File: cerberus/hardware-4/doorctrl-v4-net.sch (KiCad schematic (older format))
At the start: 40 parts, among them CON6 RJHSE-5085, U4 ENC28J60, U5 MC34063, U9 BCR08PN, X2 25MHz

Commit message: Various cleanups
git-svn-id: file:///home/ff/projects/osaa/svn@255 a092026d-3e22-4cff-94a7-eaa6fdd35d37
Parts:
- C37: value 100uF -> 220uF
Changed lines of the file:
@@
-EESchema Schematic File Version 2  date 2011-01-03T16:40:54 CET
+EESchema Schematic File Version 2  date 2011-01-17T19:42:11 CET
 LIBS:enc28j60
 LIBS:power
@@
 Sheet 2 6
 Title ""
-Date "3 jan 2011"
+Date "17 jan 2011"
 Rev ""
 Comp ""
@@
 P 6550 6450
 F 0 "C37" H 6600 6550 50  0000 L CNN
-F 1 "100uF" H 6600 6350 50  0000 L CNN
+F 1 "220uF" H 6600 6350 50  0000 L CNN
 	1    6550 6450
 	1    0    0    -1

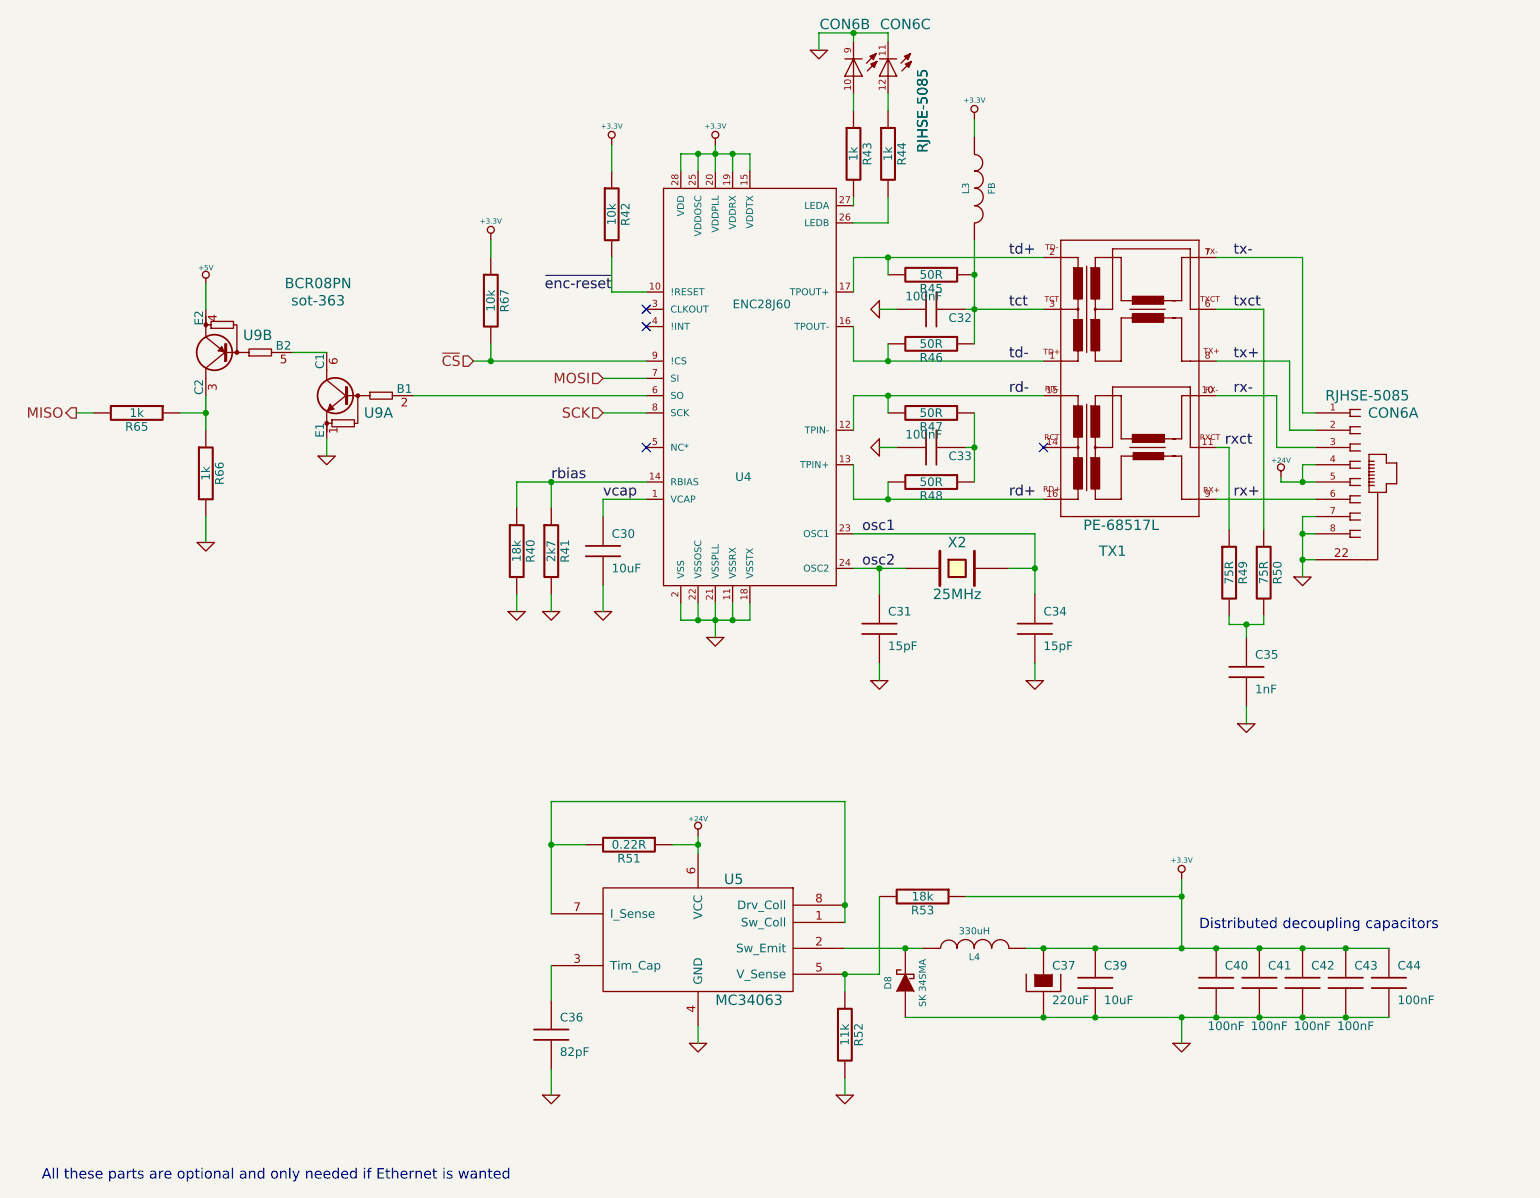
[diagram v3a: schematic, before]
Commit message: Fixed a couple of bugs: No more level shifter and rfid carrier wave output is connected correctly
git-svn-id: file:///home/ff/projects/osaa/svn@258 a092026d-3e22-4cff-94a7-eaa6fdd35d37
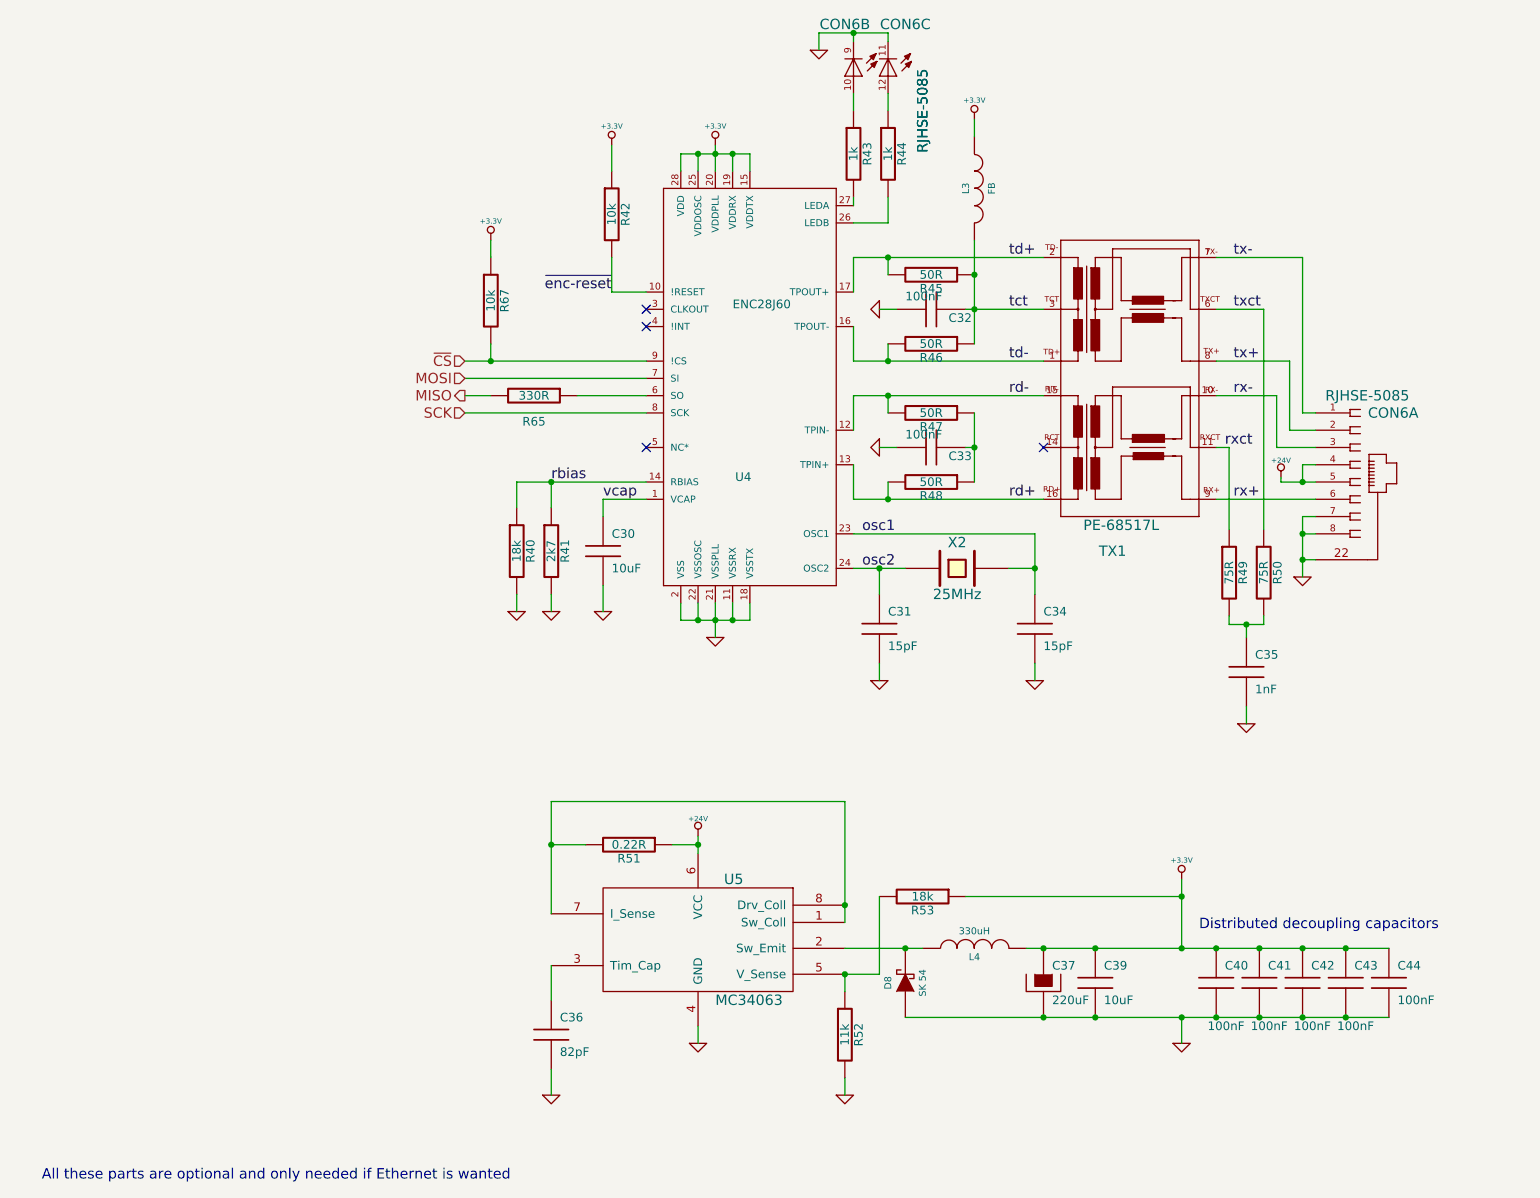
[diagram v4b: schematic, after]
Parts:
- removed R66: 1k, symbol R
- removed U9: BCR08PN, sot-363, symbol NPN/PNP
- D8: value SK 34SMA -> SK 54
- R65: value 1k -> 330R
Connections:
- net at U4.6 (SO): now also R65.1
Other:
- moved on the sheet: R65
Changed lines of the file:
@@
-EESchema Schematic File Version 2  date 2011-01-17T20:19:18 CET
+EESchema Schematic File Version 2  date 2011-01-23T22:09:23 CET
 LIBS:enc28j60
 LIBS:power
@@
 Sheet 2 6
 Title ""
-Date "17 jan 2011"
+Date "23 jan 2011"
 Rev ""
 Comp ""
@@
 $EndDescr
 Wire Wire Line
-	950  3150 1050 3150
-Wire Wire Line
-	1700 3250 1700 3050
-Wire Wire Line
-	1700 2400 1700 2550
-Wire Wire Line
-	2400 3400 2400 3300
+	3200 3050 3350 3050
 Wire Wire Line
 	3350 2150 3350 2250
 Wire Wire Line
-	3250 2850 4250 2850
-Wire Wire Line
-	6550 2550 6100 2550
-Wire Wire Line
-	6550 3050 5450 3050
+	3200 2850 3350 2850
+Wire Wire Line
+	3350 2850 4250 2850
+Wire Wire Line
+	6550 2550 6150 2550
+Wire Wire Line
+	6150 2550 6100 2550
+Wire Wire Line
+	6550 3050 5650 3050
+Wire Wire Line
+	5650 3050 5450 3050
 Connection ~ 8050 4000
 Wire Wire Line
 	8050 4000 8125 4000
 Wire Wire Line
-	8550 6250 6450 6250
-Wire Wire Line
-	7350 6250 7350 5850
+	8550 6250 8300 6250
+Wire Wire Line
+	8300 6250 8050 6250
+Wire Wire Line
+	8050 6250 7800 6250
+Wire Wire Line
+	7800 6250 7550 6250
+Wire Wire Line
+	7550 6250 7350 6250
+Wire Wire Line
+	7350 6250 6850 6250
+Wire Wire Line
+	6850 6250 6550 6250
+Wire Wire Line
+	6550 6250 6450 6250
+Wire Wire Line
+	7350 6250 7350 5950
+Wire Wire Line
+	7350 5950 7350 5850
 Connection ~ 7350 6650
 Wire Wire Line
@@
 Connection ~ 5750 6250
 Wire Wire Line
-	5850 6250 5400 6250
+	5850 6250 5750 6250
+Wire Wire Line
+	5750 6250 5400 6250
 Connection ~ 5400 6400
 Wire Wire Line
@@
 Connection ~ 5400 6000
 Wire Wire Line
-	5400 6100 5400 5400
-Wire Wire Line
-	4550 5600 4550 5700
-Wire Wire Line
-	3700 6050 3700 5400
+	5400 6100 5400 6000
+Wire Wire Line
+	5400 6000 5400 5400
+Wire Wire Line
+	4550 5600 4550 5650
+Wire Wire Line
+	4550 5650 4550 5700
+Wire Wire Line
+	3700 6050 3700 5650
+Wire Wire Line
+	3700 5650 3700 5400
 Wire Wire Line
 	3700 5400 5400 5400
@@
 	7825 4325 7825 4375
 Wire Wire Line
-	7825 4375 7625 4375
+	7825 4375 7725 4375
+Wire Wire Line
+	7725 4375 7625 4375
 Wire Wire Line
 	7725 4950 7725 4850
@@
 	8125 3650 7550 3650
 Wire Wire Line
-	6150 3150 6150 3550
+	6150 3150 6150 3350
+Wire Wire Line
+	6150 3350 6150 3550
 Connection ~ 5650 3650
 Wire Wire Line
@@
 	5650 1000 5650 950
 Wire Wire Line
-	5650 950  5250 950
+	5650 950  5450 950
+Wire Wire Line
+	5450 950  5250 950
 Wire Wire Line
 	5250 950  5250 1050
@@
 	6500 4600 6500 4700
 Wire Wire Line
-	5750 4050 5450 4050
-Wire Wire Line
-	6500 4200 6500 3850
+	5750 4050 5600 4050
+Wire Wire Line
+	5600 4050 5450 4050
+Wire Wire Line
+	6500 4200 6500 4050
+Wire Wire Line
+	6500 4050 6500 3850
 Wire Wire Line
 	6500 3850 5450 3850
@@
 	4000 3650 4000 3750
 Wire Wire Line
-	4250 3550 3500 3550
+	4250 3550 3700 3550
+Wire Wire Line
+	3700 3550 3500 3550
 Wire Wire Line
 	3500 3550 3500 3700
@@
 	4750 1750 4750 1650
 Wire Wire Line
-	4650 1600 4650 1750
+	4650 1600 4650 1650
+Wire Wire Line
+	4650 1650 4650 1750
 Wire Wire Line
 	4450 1750 4450 1650
 Connection ~ 4750 4350
 Wire Wire Line
-	4850 4350 4450 4350
+	4850 4350 4750 4350
+Wire Wire Line
+	4750 4350 4650 4350
+Wire Wire Line
+	4650 4350 4550 4350
+Wire Wire Line
+	4550 4350 4450 4350
 Wire Wire Line
 	4850 4350 4850 4250
 Connection ~ 4650 4350
 Wire Wire Line
-	4650 4250 4650 4450
+	4650 4250 4650 4350
+Wire Wire Line
+	4650 4350 4650 4450
 Wire Wire Line
 	4450 4350 4450 4250
@@
 	4850 1750 4850 1650
 Wire Wire Line
-	4850 1650 4450 1650
+	4850 1650 4750 1650
+Wire Wire Line
+	4750 1650 4650 1650
+Wire Wire Line
+	4650 1650 4550 1650
+Wire Wire Line
+	4550 1650 4450 1650
 Connection ~ 4650 1650
 Wire Wire Line
@@
 	5650 1300 5650 1400
 Wire Wire Line
-	6150 2150 6150 2750
+	6150 2150 6150 2350
+Wire Wire Line
+	6150 2350 6150 2550
+Wire Wire Line
+	6150 2550 6150 2750
 Connection ~ 6150 2350
 Wire Wire Line
@@
 	7925 3525 7925 3550
 Wire Wire Line
-	7925 3550 8125 3550
+	7925 3550 8050 3550
+Wire Wire Line
+	8050 3550 8125 3550
 Connection ~ 8050 3550
 Wire Wire Line
-	5750 6650 8550 6650
-Wire Wire Line
-	8050 3750 8050 4100
-Wire Wire Line
-	5450 3650 6550 3650
-Wire Wire Line
-	5450 2850 6550 2850
-Wire Wire Line
-	5450 2250 6550 2250
-Wire Wire Line
-	4250 3150 4000 3150
-Wire Wire Line
-	4250 2950 4000 2950
+	5750 6650 6550 6650
+Wire Wire Line
+	6550 6650 6850 6650
+Wire Wire Line
+	6850 6650 7350 6650
+Wire Wire Line
+	7350 6650 7550 6650
+Wire Wire Line
+	7550 6650 7800 6650
+Wire Wire Line
+	7800 6650 8050 6650
+Wire Wire Line
+	8050 6650 8300 6650
+Wire Wire Line
+	8300 6650 8550 6650
+Wire Wire Line
+	8050 3750 8050 3850
+Wire Wire Line
+	8050 3850 8050 4000
+Wire Wire Line
+	8050 4000 8050 4100
+Wire Wire Line
+	5450 3650 5650 3650
+Wire Wire Line
+	5650 3650 6550 3650
+Wire Wire Line
+	5450 2850 5650 2850
+Wire Wire Line
+	5650 2850 6550 2850
+Wire Wire Line
+	5450 2250 5650 2250
+Wire Wire Line
+	5650 2250 6550 2250
+Wire Wire Line
+	4250 3150 3200 3150
+Wire Wire Line
+	4250 2950 3200 2950
 Wire Wire Line
 	3350 2750 3350 2850
 Connection ~ 3350 2850
 Wire Wire Line
-	2900 3050 4250 3050
-Wire Wire Line
-	2400 2800 2200 2800
-Wire Wire Line
-	1700 3750 1700 3900
-Wire Wire Line
-	1550 3150 1700 3150
-Connection ~ 1700 3150
-$Comp
-L GND #PWR017
-U 1 1 4D21B7E7
-P 1700 3900
-F 0 "#PWR017" H 1700 3900 30  0001 C CNN
-F 1 "GND" H 1700 3830 30  0001 C CNN
-	1    1700 3900
-	1    0    0    -1
-$EndComp
-$Comp
-L R R66
-U 1 1 4D21B7DC
-P 1700 3500
-F 0 "R66" V 1780 3500 50  0000 C CNN
-F 1 "1k" V 1700 3500 50  0000 C CNN
-	1    1700 3500
-	1    0    0    -1
-$EndComp
-$Comp
-L GND #PWR018
-U 1 1 4D21B758
-P 2400 3400
-F 0 "#PWR018" H 2400 3400 30  0001 C CNN
-F 1 "GND" H 2400 3330 30  0001 C CNN
-	1    2400 3400
-	1    0    0    -1
-$EndComp
-$Comp
-L NPN/PNP U9
-U 2 1 4D21B725
-P 1750 2800
-F 0 "U9" H 2000 2700 60  0000 C CNN
-F 1 "BCR08PN" H 2350 2400 60  0000 C CNN
-F 2 "sot-363" H 2350 2500 60  0000 C CNN
-	2    1750 2800
-	1    0    0    1
-$EndComp
-$Comp
-L NPN/PNP U9
-U 1 1 4D21B6EA
-P 2450 3050
-F 0 "U9" H 2700 2950 60  0000 C CNN
-F 1 "BCR08PN" H 2650 3200 60  0001 C CNN
-F 2 "sot-363" H 2700 3250 60  0001 C CNN
-	1    2450 3050
-	1    0    0    -1
-$EndComp
+	3850 3050 4250 3050
 $Comp
 L R R65
 U 1 1 4D21A96D
-P 1300 3150
-F 0 "R65" V 1380 3150 50  0000 C CNN
-F 1 "1k" V 1300 3150 50  0000 C CNN
-	1    1300 3150
-	0    1    1    0
-$EndComp
-$Comp
-L +5V #PWR019
-U 1 1 4D21A730
-P 1700 2400
-F 0 "#PWR019" H 1700 2490 20  0001 C CNN
-F 1 "+5V" H 1700 2490 30  0000 C CNN
-	1    1700 2400
-	1    0    0    -1
+P 3600 3050
+F 0 "R65" V 3750 3050 50  0000 C CNN
+F 1 "330R" V 3600 3050 50  0000 C CNN
+	1    3600 3050
+	0    1    1    0
 $EndComp
 $Comp
@@
 P 5750 6450
 F 0 "D8" H 5750 6550 40  0000 C CNN
-F 1 "SK 34SMA" H 5750 6350 40  0000 C CNN
+F 1 "SK 54" H 5750 6350 40  0000 C CNN
 	1    5750 6450
 	0    -1   -1   0
@@
 	1    0    0    -1
 $EndComp
-Text HLabel 4000 3150 0    60   Input ~ 0
+Text HLabel 3200 3150 0    60   Input ~ 0
 SCK
-Text HLabel 950  3150 0    60   Output ~ 0
+Text HLabel 3200 3050 0    60   Output ~ 0
 MISO
-Text HLabel 4000 2950 0    60   Input ~ 0
+Text HLabel 3200 2950 0    60   Input ~ 0
 MOSI
-Text HLabel 3250 2850 0    60   Input ~ 0
+Text HLabel 3200 2850 0    60   Input ~ 0
 ~CS
 $Comp
